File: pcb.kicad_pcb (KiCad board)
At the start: 2 copper layers, 30 x 62 mm, 34 parts, among them J1 4.5-18V, Q1 FDN339AN, SW1 SW_SPST, U1 WeMos_D1_mini, U2 TSOP38236, U3 TPS54302, U4 AP131-18, U5 SGP30, U6 AHT20, U7 PCA9306DC1

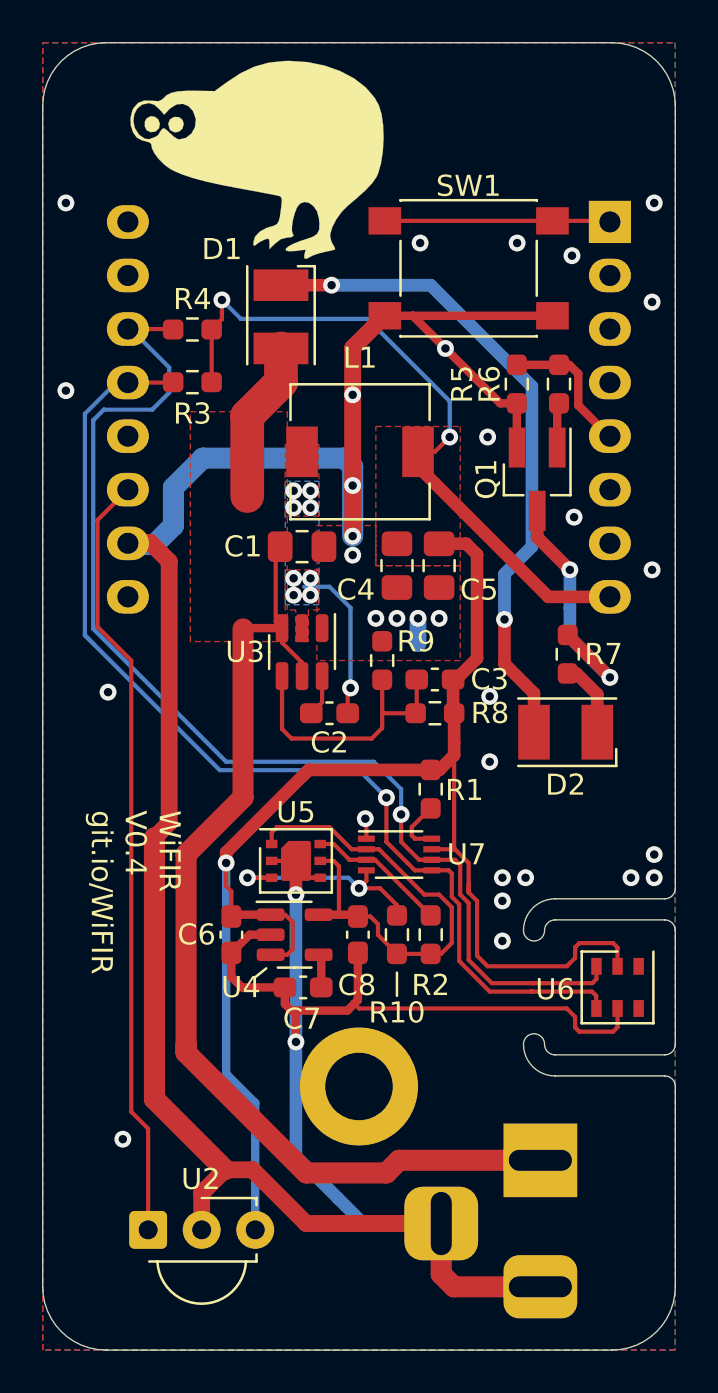
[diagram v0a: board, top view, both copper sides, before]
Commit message: Use 220uH inductor and emitter follower LED driver
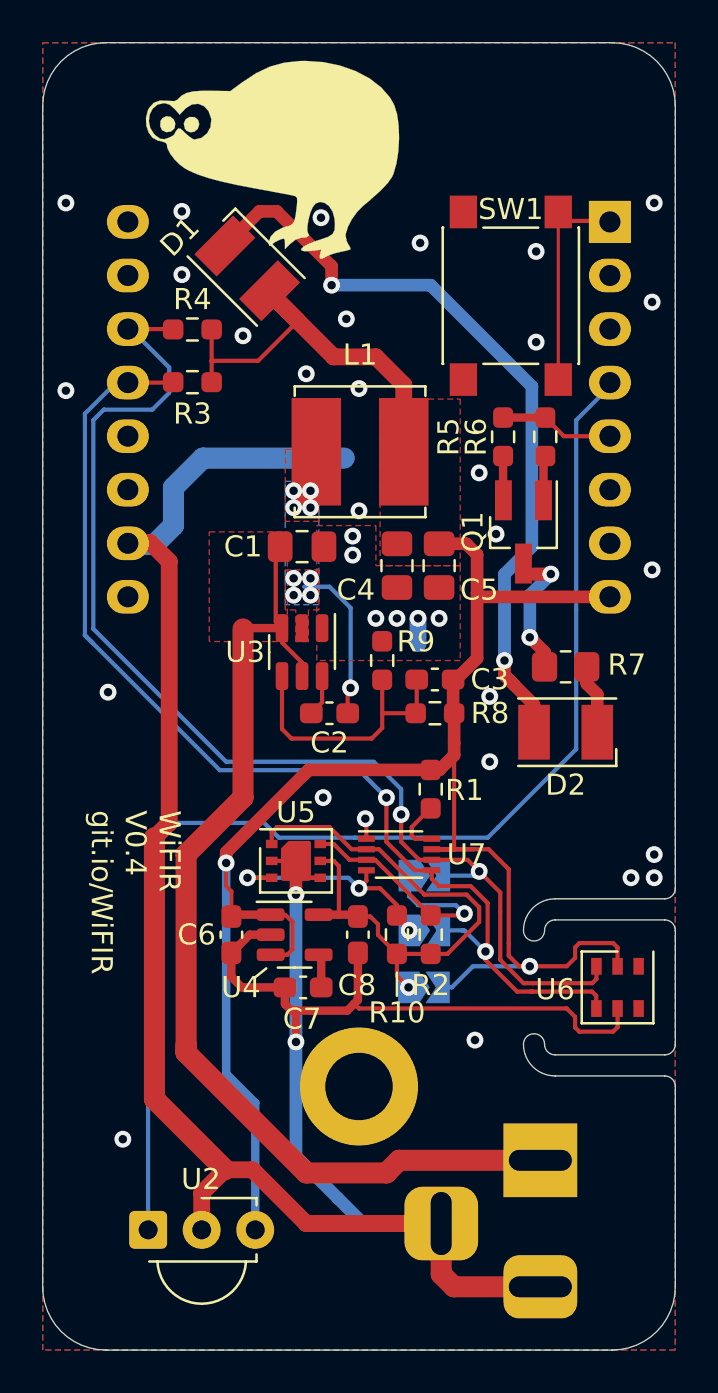
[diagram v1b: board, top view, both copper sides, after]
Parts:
- added JP1: 1v8-bp, Jumper:SolderJumper-2_P1.3mm_Open_TrianglePad1.0x1.5mm, B.Cu at (158.1, 117.8)
- added JP2: sda-bp, Jumper:SolderJumper-2_P1.3mm_Open_TrianglePad1.0x1.5mm, B.Cu at (158.1, 112.5)
- added JP3: scl-bp, Jumper:SolderJumper-2_P1.3mm_Open_TrianglePad1.0x1.5mm, B.Cu at (158.1, 115.1)
- J1: value 4.5-18V -> 12V
- L1: value 6.8uH -> 100μH; footprint Inductor_SMD:L_6.3x6.3_H3 -> Inductor_SMD:L_Bourns_SRN6045TA
- R7: value 27R -> 1R5; footprint Resistor_SMD:R_0603_1608Metric_Pad0.98x0.95mm_HandSolder -> Resistor_SMD:R_0805_2012Metric_Pad1.20x1.40mm_HandSolder
- moved D1 2.80 mm to (149.7, 83.7), turned to -45 degrees
- moved R5 2.58 mm to (161.8, 91.7)
- moved R6 2.58 mm to (163.8, 91.7)
- moved Q1 2.58 mm to (162.8, 96.2)
- moved SW1 2.39 mm to (162.2, 85.0), turned to 90 degrees
- moved G*** 0.73 mm to (153.4, 76.7)
- moved R7 0.61 mm to (164.8, 102.6), turned to 180 degrees
- moved G*** 0.33 mm to (147.6, 116.2)
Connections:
- D1 pad 2: VCC -> +3V3
- U1 pad 11: IR_SIGNAL -> unconnected-(U1-Pad11)
- U1 pad 4: unconnected-(U1-Pad4) -> IR_SIGNAL
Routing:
- net GND: track 159.9 -> 129.5 mm, vias 33 -> 36
- net IR_SIGNAL: track 36.7 -> 59.0 mm
- net VCC: track 57.3 -> 49.6 mm
- net Net-(D1-Pad1): track 31.4 -> 37.4 mm
- net /SCL_1V8: track 6.64 -> 12.2 mm, vias 0 -> 1
- net Net-(Q1-Pad3): track 12.2 -> 7.20 mm
- net +1V8: track 23.4 -> 27.2 mm, vias 0 -> 1
- net +3V3: track 105.1 -> 107.7 mm, vias 3 -> 2
- net /SDA_3V3: track 51.4 -> 53.7 mm, vias 1 -> 2
- net /SCL_3V3: track 55.5 -> 56.9 mm, vias 1 -> 2
- net IR_BLAST: track 6.72 -> 5.50 mm
- net /SDA_1V8: track 10.5 -> 11.4 mm, vias 2 -> 3
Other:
- board text added: "1v8->3v3 bypass"
